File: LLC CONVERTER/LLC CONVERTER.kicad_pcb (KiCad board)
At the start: 2 copper layers, 1 part, among them IC1 UCC256601DDBR

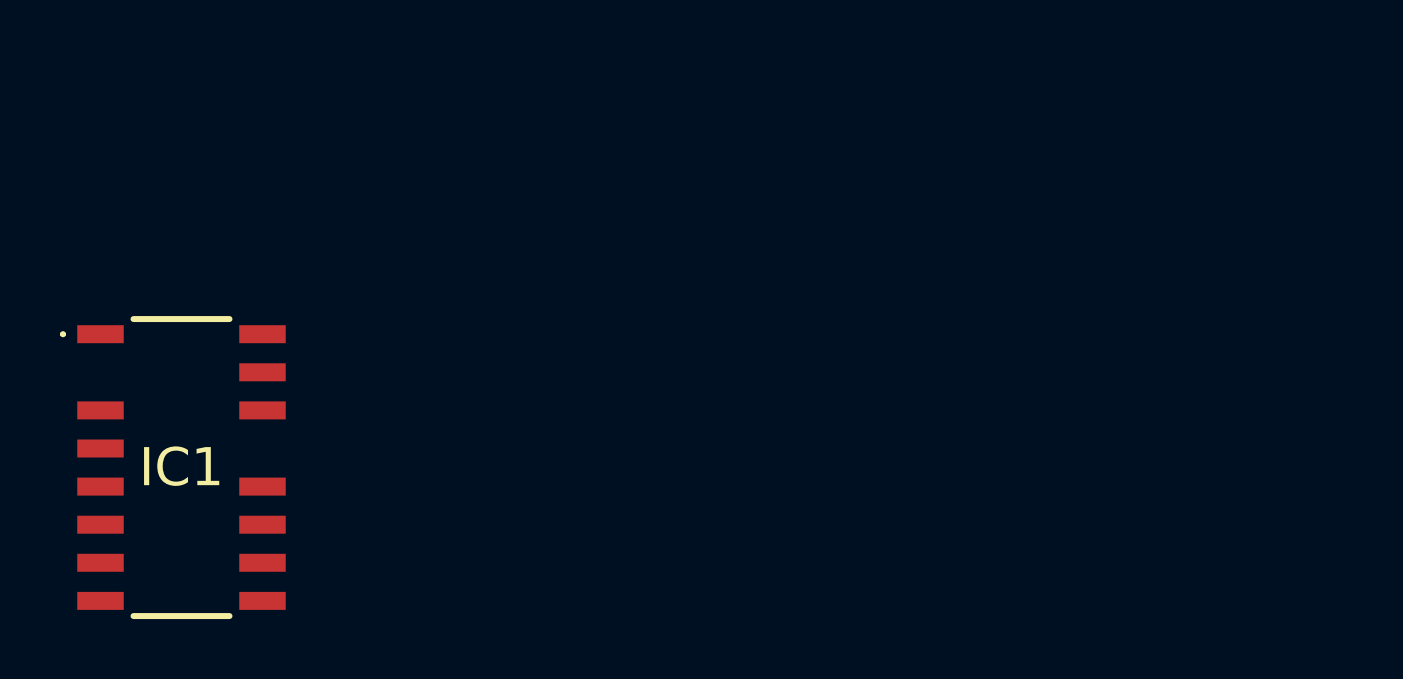
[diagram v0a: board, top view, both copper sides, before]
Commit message: update: changed pcb position
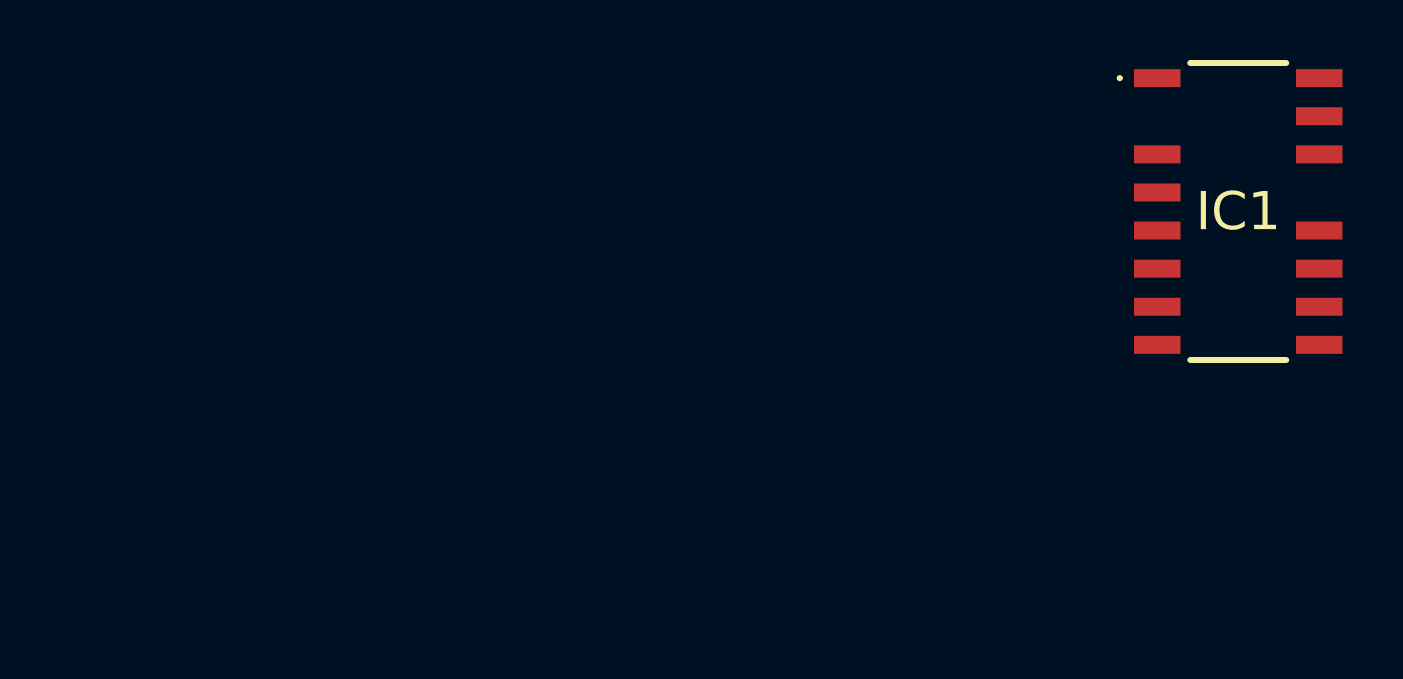
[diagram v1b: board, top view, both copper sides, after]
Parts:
- moved IC1 36.2 mm to (173.1, 84.7)
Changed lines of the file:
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@@
 	(footprint "PCB:UCC256601DDBR"
 		(layer "F.Cu")
-		(at 137.825 93.28)
+		(at 173.05 84.745)
 		(descr "UCC256601DDBR-2")
 		(tags "Integrated Circuit")

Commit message: change kiya
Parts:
- moved IC1 102.3 mm to (71.9, 69.8)
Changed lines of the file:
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@@
 	(footprint "PCB:UCC256601DDBR"
 		(layer "F.Cu")
-		(at 173.05 84.745)
+		(at 71.9 69.78)
 		(descr "UCC256601DDBR-2")
 		(tags "Integrated Circuit")
